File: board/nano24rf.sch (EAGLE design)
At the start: 20 parts

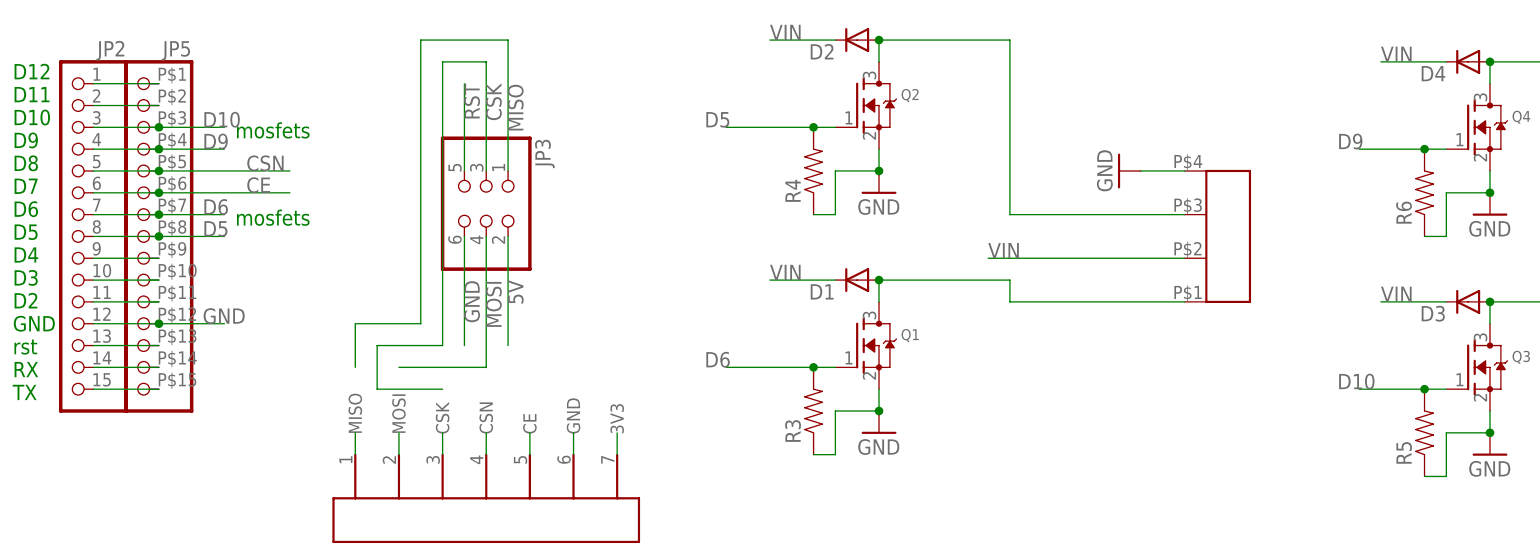
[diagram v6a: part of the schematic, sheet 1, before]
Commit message: switched to pin11 one of the mosfet
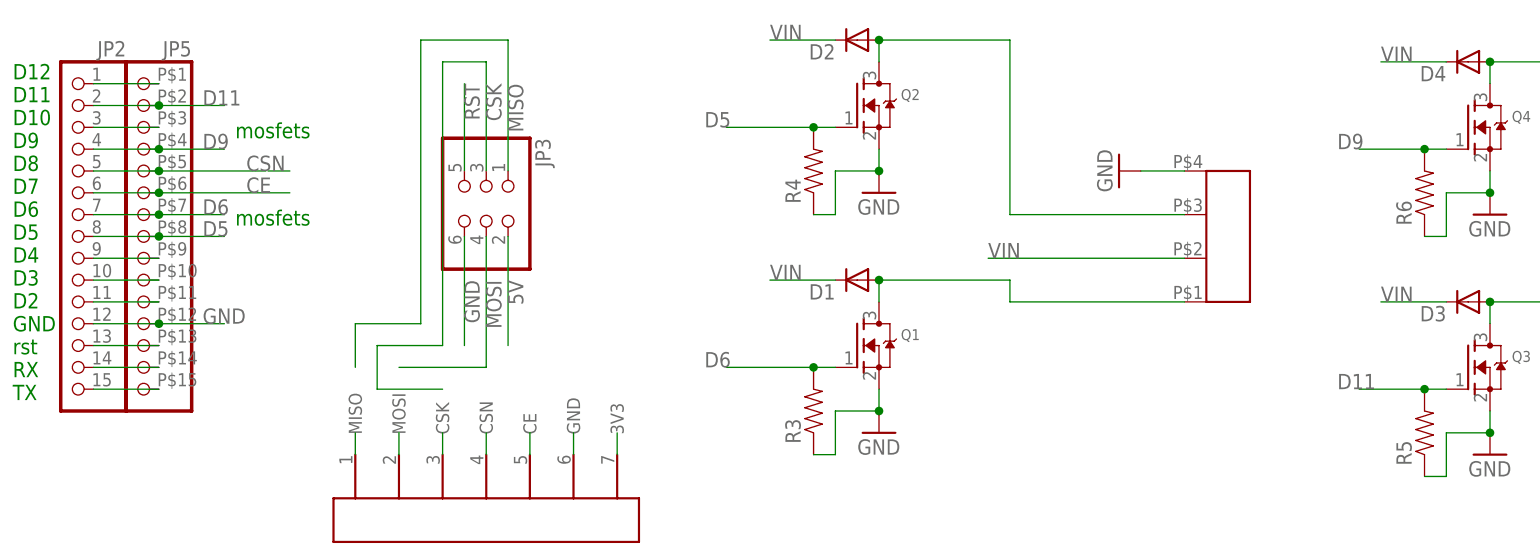
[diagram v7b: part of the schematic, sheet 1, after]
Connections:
- removed net N$19: JP2.2, JP5.2
- new net D11: JP2.2, JP5.2, Q3.G, R5.2
- net D10: no longer Q3.G, R5.2
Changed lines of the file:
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@@
 <pinref part="JP2" gate="G$1" pin="3"/>
 <wire x1="68.58" y1="60.96" x2="76.2" y2="60.96" width="0.1524" layer="91"/>
-<label x="81.28" y="60.96" size="1.778" layer="95"/>
 <pinref part="JP5" gate="G$1" pin="3"/>
-<wire x1="76.2" y1="60.96" x2="83.82" y2="60.96" width="0.1524" layer="91"/>
-<junction x="76.2" y="60.96"/>
-</segment>
-<segment>
-<label x="213.36" y="30.48" size="1.778" layer="95"/>
-<pinref part="Q3" gate="G$1" pin="G"/>
-<wire x1="223.52" y1="30.48" x2="226.06" y2="30.48" width="0.1524" layer="91"/>
-<pinref part="R5" gate="G$1" pin="2"/>
-<wire x1="215.9" y1="30.48" x2="223.52" y2="30.48" width="0.1524" layer="91"/>
-<junction x="223.52" y="30.48"/>
 </segment>
 </net>
@@
 </segment>
 </net>
-<net name="N$19" class="0">
+<net name="N$20" class="0">
+<segment>
+<pinref part="JP5" gate="G$1" pin="1"/>
+<pinref part="JP2" gate="G$1" pin="1"/>
+<wire x1="76.2" y1="66.04" x2="68.58" y2="66.04" width="0.1524" layer="91"/>
+</segment>
+</net>
+<net name="D11" class="0">
 <segment>
 <pinref part="JP2" gate="G$1" pin="2"/>
 <pinref part="JP5" gate="G$1" pin="2"/>
 <wire x1="68.58" y1="63.5" x2="76.2" y2="63.5" width="0.1524" layer="91"/>
-</segment>
-</net>
-<net name="N$20" class="0">
-<segment>
-<pinref part="JP5" gate="G$1" pin="1"/>
-<pinref part="JP2" gate="G$1" pin="1"/>
-<wire x1="76.2" y1="66.04" x2="68.58" y2="66.04" width="0.1524" layer="91"/>
-</segment>
-</net>
+<wire x1="76.2" y1="63.5" x2="83.82" y2="63.5" width="0.1524" layer="91"/>
+<junction x="76.2" y="63.5"/>
+<label x="81.28" y="63.5" size="1.778" layer="95"/>
+</segment>
+<segment>
+<label x="213.36" y="30.48" size="1.778" layer="95"/>
+<pinref part="Q3" gate="G$1" pin="G"/>
+<wire x1="223.52" y1="30.48" x2="226.06" y2="30.48" width="0.1524" layer="91"/>
+<pinref part="R5" gate="G$1" pin="2"/>
+<wire x1="215.9" y1="30.48" x2="223.52" y2="30.48" width="0.1524" layer="91"/>
+<junction x="223.52" y="30.48"/>
+</segment>
+</net>

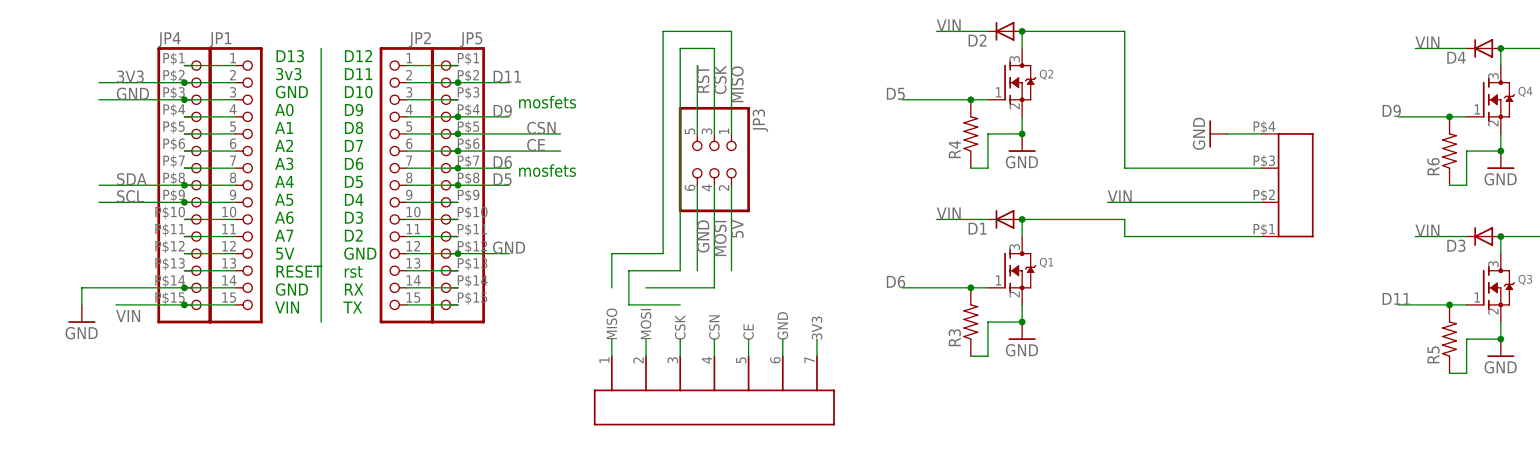
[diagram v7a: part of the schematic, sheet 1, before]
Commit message: removed SPI
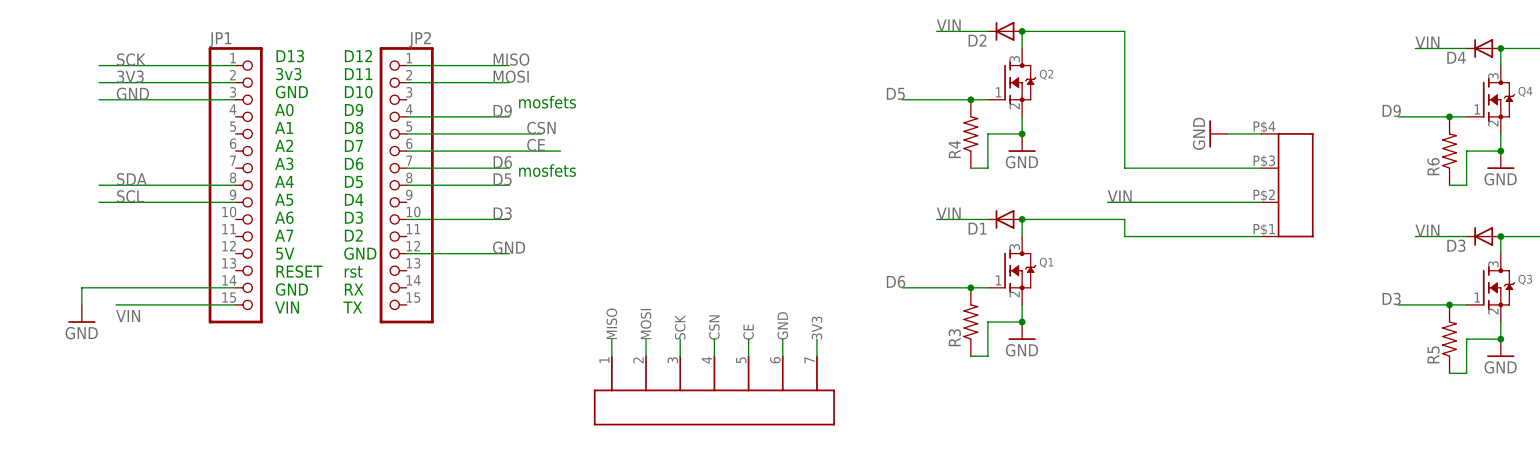
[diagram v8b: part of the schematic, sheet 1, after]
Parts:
- removed JP3: (no value), nano24rf:PINHD-2X3SMT
- removed JP4, JP5: (no value), nano24rf:HEADER-1X15LONG
- MOSFET-12, MOSFET-34: value FATPAD4LONG -> FATPAD4SEQ; device nano24rf:FATPAD4LONG -> nano24rf:FATPAD4SEQ
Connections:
- removed net 5V: JP3.2
- removed net D10: JP2.3, JP5.3
- removed net D11: JP2.2, JP5.2, Q3.G, R5.2
- removed net N$10: JP1.11, JP4.11
- removed net N$11: JP1.12, JP4.12
- removed net N$12: JP1.13, JP4.13
- removed net N$13: JP2.15, JP5.15
- removed net N$14: JP2.14, JP5.14
- removed net N$15: JP2.13, JP5.13
- removed net N$16: JP2.11, JP5.11
- removed net N$17: JP2.10, JP5.10
- removed net N$18: JP2.9, JP5.9
- removed net N$20: JP2.1, JP5.1
- removed net N$4: JP1.1, JP4.1
- removed net N$5: JP1.4, JP4.4
- removed net N$6: JP1.5, JP4.5
- removed net N$7: JP1.6, JP4.6
- removed net N$8: JP1.7, JP4.7
- removed net N$9: JP1.10, JP4.10
- removed net RST: JP3.5
- new net D3: JP2.10, Q3.G, R5.2
- new net SCK: JP1.1
- net 3V3: no longer JP4.2
- net CE: no longer JP5.6
- net CSK: now also RF24.SCK; no longer JP3.3, RF24.CSK
- net CSN: no longer JP5.5
- net D5: no longer JP5.8
- net D6: no longer JP5.7
- net D9: no longer JP5.4
- net GND: no longer JP3.6, JP4.14, JP4.3, JP5.12
- net MISO: now also JP2.1; no longer JP3.1
- net MOSI: now also JP2.2; no longer JP3.4
- net SCL: no longer JP4.9
- net SDA: no longer JP4.8
- net VIN: no longer JP4.15
